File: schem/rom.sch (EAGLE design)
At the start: 14 parts, among them IC10 74HC32N, IC11 74HC32N, IC12 74HC32N, IC13 74HC32N, IC14 74HC04N, IC6 74HC374N, IC7 74HC08N, IC8 74HC377N, IC9 74HC377N

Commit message: progress
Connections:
- net IRQ renamed /IRQ
- new net SYNC: IC7D.O
- net /BUSACK: now also IC7D.I0
- net FETCH: now also IC7D.I1
- net INVF: no longer IC7C.O
- net INVF0: now also IC7C.O
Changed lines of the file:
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@@
 <instance part="IC13" gate="B" x="269.24" y="-15.24"/>
 <instance part="IC13" gate="C" x="154.94" y="-20.32"/>
+<instance part="IC7" gate="D" x="228.6" y="20.32"/>
 </instances>
 <busses>
@@
 </segment>
 </net>
-<net name="IRQ" class="0">
+<net name="/IRQ" class="0">
 <segment>
 <pinref part="IC6" gate="A" pin="4D"/>
@@
 <wire x1="220.98" y1="48.26" x2="210.82" y2="48.26" width="0.1524" layer="91"/>
 <label x="210.82" y="48.26" size="1.778" layer="95"/>
+</segment>
+<segment>
+<pinref part="IC7" gate="D" pin="I0"/>
+<wire x1="220.98" y1="22.86" x2="210.82" y2="22.86" width="0.1524" layer="91"/>
+<label x="210.82" y="22.86" size="1.778" layer="95"/>
 </segment>
 </net>
@@
 <label x="276.86" y="45.72" size="1.778" layer="95"/>
 </segment>
+<segment>
+<pinref part="IC7" gate="D" pin="I1"/>
+<wire x1="220.98" y1="17.78" x2="213.36" y2="17.78" width="0.1524" layer="91"/>
+<label x="213.36" y="17.78" size="1.778" layer="95"/>
+</segment>
 </net>
 <net name="/INRES" class="0">
@@
 <label x="226.06" y="83.82" size="1.778" layer="95"/>
 </segment>
+<segment>
+<pinref part="IC7" gate="C" pin="O"/>
+<wire x1="236.22" y1="33.02" x2="246.38" y2="33.02" width="0.1524" layer="91"/>
+<label x="236.22" y="33.02" size="1.778" layer="95"/>
+</segment>
 </net>
 <net name="INVF" class="0">
@@
 <label x="264.16" y="83.82" size="1.778" layer="95"/>
 </segment>
-<segment>
-<pinref part="IC7" gate="C" pin="O"/>
-<wire x1="236.22" y1="33.02" x2="246.38" y2="33.02" width="0.1524" layer="91"/>
-<label x="236.22" y="33.02" size="1.778" layer="95"/>
-</segment>
-</net>
+</net>
+<net name="SYNC" class="0">
+<segment>
+<pinref part="IC7" gate="D" pin="O"/>
+<wire x1="236.22" y1="20.32" x2="243.84" y2="20.32" width="0.1524" layer="91"/>
+<label x="236.22" y="20.32" size="1.778" layer="95"/>
+</segment>
+</net>

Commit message: board changes ; rom schematic finished
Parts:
- added SV1, SV3, SV4, SV6, SV7, SV8: (no value), con-lstb:MA08-1
- added SV10, SV2, SV5, SV9: (no value), con-lstb:MA06-1
- added SV11, SV12, SV13: (no value), con-lstb:MA05-2
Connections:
- removed net IBS0: IC2A.O0
- removed net IBS1: IC2A.O1
- removed net IBS2: IC2A.O2
- removed net IBS3: IC2A.O3
- new net IB0: SV1.1
- new net IB1: SV1.2
- new net IB2: SV1.3
- new net IB3: SV1.4
- new net IB4: SV1.5
- new net IB5: SV1.6
- new net IB6: SV1.7
- new net IB7: SV1.8
- new net IBR0: IC2A.O0, SV10.3
- new net IBR1: IC2A.O1, SV10.4
- new net IBR2: IC2A.O2, SV10.5
- new net IBR3: IC2A.O3, SV10.6
- new net OB0: SV4.1
- new net OB1: SV4.2
- new net OB2: SV4.3
- new net OB3: SV4.4
- new net OB4: SV4.5
- new net OB5: SV4.6
- new net OB6: SV4.7
- new net OB7: SV4.8
- net /BUSACK: now also SV9.2
- net /BUSREQ: now also SV9.3
- net /INRES: now also SV12.3
- net /IRQ: now also SV9.6
- net /WE: now also SV9.4
- net ABHS0: now also SV11.2
- net ABHS1: now also SV11.4
- net ABHS2: now also SV11.6
- net ABLS0: now also SV12.2
- net ABLS1: now also SV12.4
- net ABLS2: now also SV12.6
- net ALUC: now also SV8.3
- net BUSACK: now also SV9.1
- net CIN: now also SV6.8
- net CLK: now also SV2.3
- net COND: now also SV8.7
- net DB0: now also SV3.1
- net DB1: now also SV3.2
- net DB2: now also SV3.3
- net DB3: now also SV3.4
- net DB4: now also SV3.5
- net DB5: now also SV3.6
- net DB6: now also SV3.7
- net DB7: now also SV3.8
- net DP: now also SV12.1
- net F0: now also SV6.1
- net F1: now also SV6.2
- net F2: now also SV6.3
- net F3: now also SV6.4
- net F4: now also SV6.5
- net F5: now also SV6.6
- net FL0: now also SV7.1
- net FL1: now also SV7.2
- net FL2: now also SV7.3
- net FL3: now also SV7.4
- net FL4: now also SV7.5
- net FL5: now also SV7.6
- net FL6: now also SV7.7
- net FL7: now also SV7.8
- net FL8: now also SV8.1
- net FL9: now also SV8.2
- net GND: now also IC13D.I0, IC13D.I1, IC14F.I, SV11.10, SV11.9, SV12.10, SV12.5, SV12.7, SV12.9, SV13.10, SV13.9, SV2.4, SV2.5, SV2.6, SV5.4, SV5.5, SV5.6, SV8.8
- net IN0: now also SV13.1
- net IN1: now also SV13.2
- net IN2: now also SV13.3
- net IN3: now also SV13.4
- net IN4: now also SV13.5
- net IN5: now also SV13.6
- net IN6: now also SV13.7
- net IN7: now also SV13.8
- net INIRQ: now also SV8.6
- net INVF: now also SV6.7
- net OBS0: now also SV11.1
- net OBS1: now also SV11.3
- net OBS2: now also SV11.5
- net OBS3: now also SV11.7
- net PCP: now also SV11.8, SV12.8
- net PQ0: now also SV8.4
- net PQ2: now also SV8.5
- net RESET: now also SV10.1
- net SYNC: now also SV10.2
- net VCC: now also SV2.1, SV2.2, SV5.1, SV5.2, SV5.3
- net WR: now also SV9.5

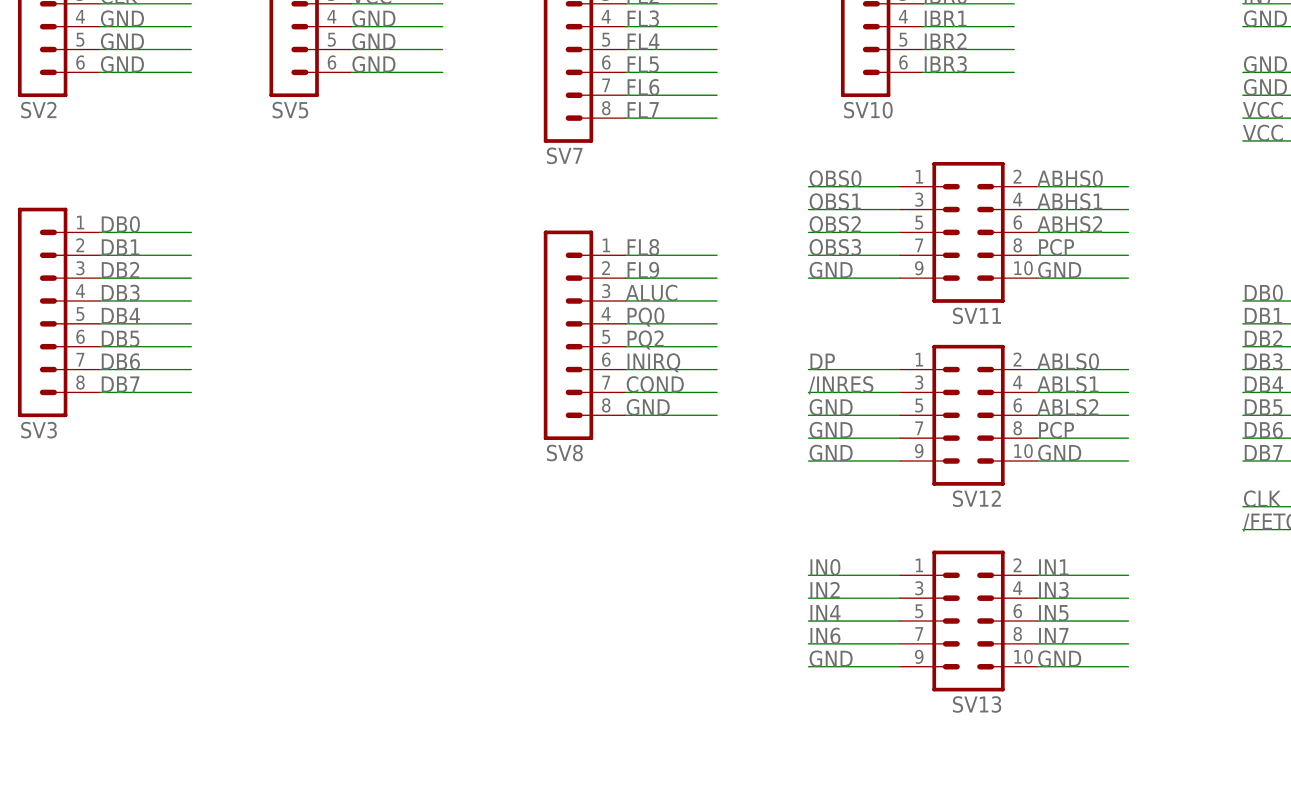
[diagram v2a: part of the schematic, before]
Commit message: adapted schematics for single headers
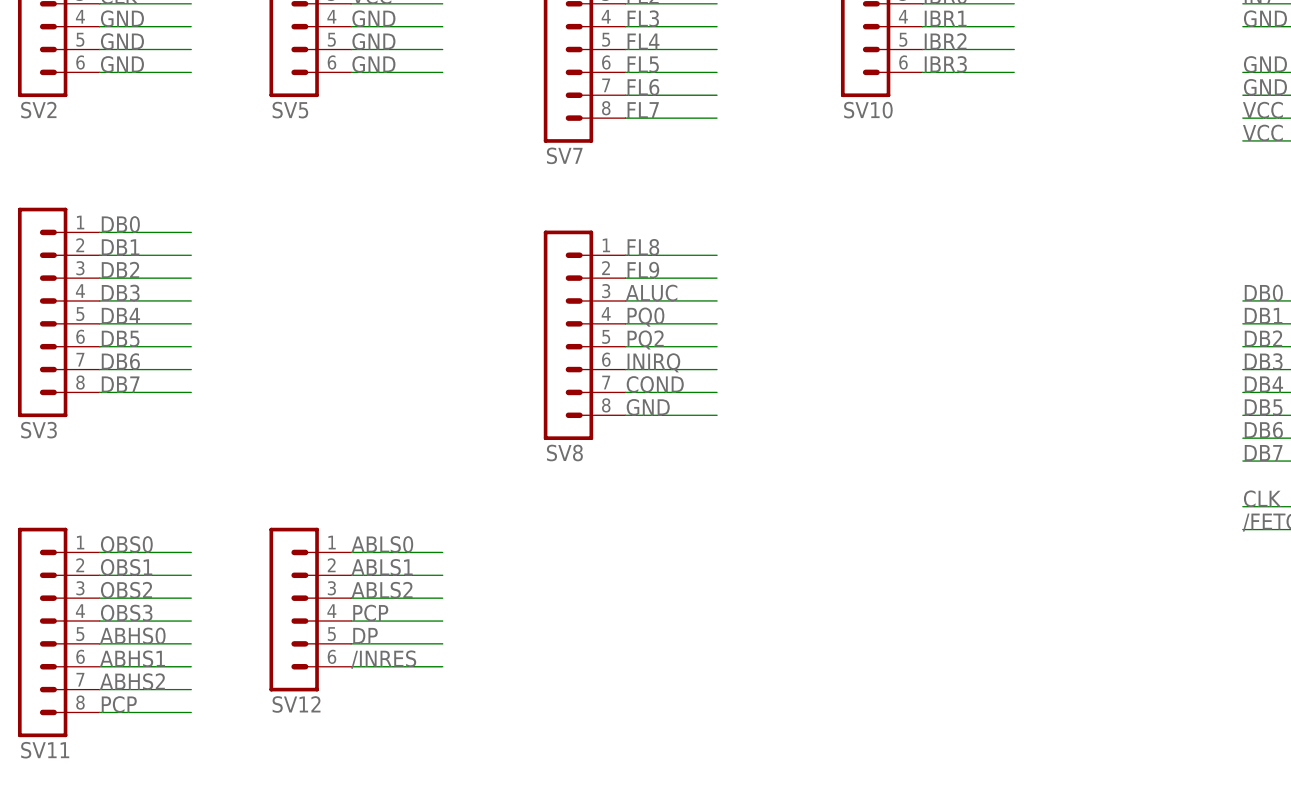
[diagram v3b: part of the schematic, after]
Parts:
- removed SV13: (no value), con-lstb:MA05-2
- SV11: device con-lstb:MA05-2 -> con-lstb:MA08-1
- SV12: device con-lstb:MA05-2 -> con-lstb:MA06-1
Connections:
- net /INRES: now also SV12.6; no longer SV12.3
- net ABHS0: now also SV11.5; no longer SV11.2
- net ABHS1: now also SV11.6; no longer SV11.4
- net ABHS2: now also SV11.7; no longer SV11.6
- net ABLS0: now also SV12.1; no longer SV12.2
- net ABLS1: now also SV12.2; no longer SV12.4
- net ABLS2: now also SV12.3; no longer SV12.6
- net DP: now also SV12.5; no longer SV12.1
- net GND: no longer SV11.10, SV11.9, SV12.10, SV12.5, SV12.7, SV12.9, SV13.10, SV13.9
- net IN0: no longer SV13.1
- net IN1: no longer SV13.2
- net IN2: no longer SV13.3
- net IN3: no longer SV13.4
- net IN4: no longer SV13.5
- net IN5: no longer SV13.6
- net IN6: no longer SV13.7
- net IN7: no longer SV13.8
- net OBS1: now also SV11.2; no longer SV11.3
- net OBS2: now also SV11.3; no longer SV11.5
- net OBS3: now also SV11.4; no longer SV11.7
- net PCP: now also SV12.4; no longer SV12.8

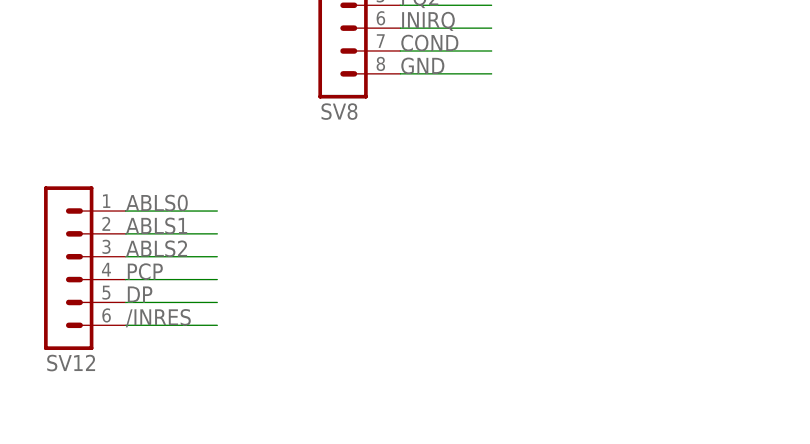
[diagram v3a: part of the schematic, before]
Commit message: added debugging pins to rom board
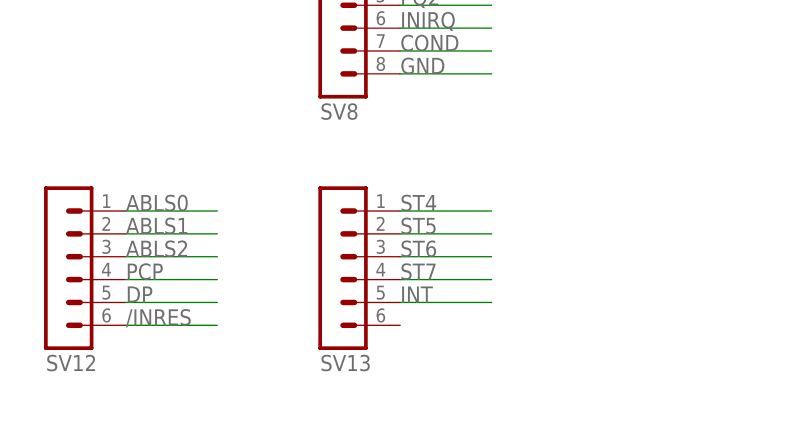
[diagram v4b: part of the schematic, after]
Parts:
- added SV13: (no value), con-lstb:MA06-1
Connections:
- net INT: now also SV13.5
- net ST4: now also SV13.1
- net ST5: now also SV13.2
- net ST6: now also SV13.3
- net ST7: now also SV13.4
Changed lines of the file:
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@@
 <part name="SV11" library="con-lstb" deviceset="MA08-1" device=""/>
 <part name="SV12" library="con-lstb" deviceset="MA06-1" device=""/>
+<part name="SV13" library="con-lstb" deviceset="MA06-1" device=""/>
 </parts>
 <sheets>
@@
 <instance part="SV11" gate="1" x="-129.54" y="-12.7" rot="MR180"/>
 <instance part="SV12" gate="1" x="-101.6" y="-12.7" rot="MR180"/>
+<instance part="SV13" gate="1" x="-71.12" y="-12.7" rot="MR180"/>
 </instances>
 <busses>
@@
 <label x="132.08" y="22.86" size="1.778" layer="95"/>
 </segment>
+<segment>
+<pinref part="SV13" gate="1" pin="1"/>
+<wire x1="-63.5" y1="-5.08" x2="-53.34" y2="-5.08" width="0.1524" layer="91"/>
+<label x="-63.5" y="-5.08" size="1.778" layer="95"/>
+</segment>
 </net>
 <net name="ST5" class="0">
@@
 <label x="132.08" y="17.78" size="1.778" layer="95"/>
 </segment>
+<segment>
+<pinref part="SV13" gate="1" pin="2"/>
+<wire x1="-63.5" y1="-7.62" x2="-53.34" y2="-7.62" width="0.1524" layer="91"/>
+<label x="-63.5" y="-7.62" size="1.778" layer="95"/>
+</segment>
 </net>
 <net name="ST6" class="0">
@@
 <label x="132.08" y="7.62" size="1.778" layer="95"/>
 </segment>
+<segment>
+<pinref part="SV13" gate="1" pin="3"/>
+<wire x1="-63.5" y1="-10.16" x2="-53.34" y2="-10.16" width="0.1524" layer="91"/>
+<label x="-63.5" y="-10.16" size="1.778" layer="95"/>
+</segment>
 </net>
 <net name="ST7" class="0">
@@
 <wire x1="132.08" y1="2.54" x2="139.7" y2="2.54" width="0.1524" layer="91"/>
 <label x="132.08" y="2.54" size="1.778" layer="95"/>
+</segment>
+<segment>
+<pinref part="SV13" gate="1" pin="4"/>
+<wire x1="-63.5" y1="-12.7" x2="-53.34" y2="-12.7" width="0.1524" layer="91"/>
+<label x="-63.5" y="-12.7" size="1.778" layer="95"/>
 </segment>
 </net>
@@
 <label x="276.86" y="7.62" size="1.778" layer="95"/>
 </segment>
-</net>
+<segment>
+<pinref part="SV13" gate="1" pin="5"/>
+<wire x1="-63.5" y1="-15.24" x2="-53.34" y2="-15.24" width="0.1524" layer="91"/>
+<label x="-63.5" y="-15.24" size="1.778" layer="95"/>
+</segment>
+</net>

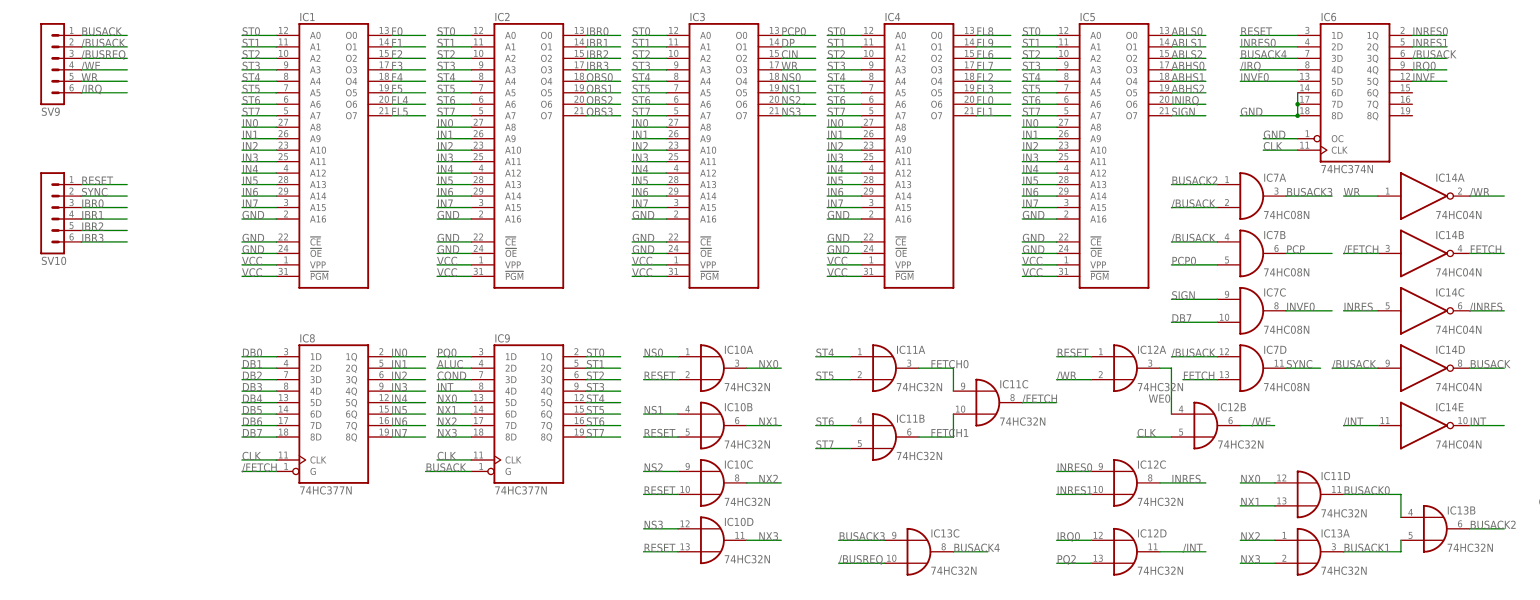
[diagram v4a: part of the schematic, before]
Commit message: added synchronizer to reset line
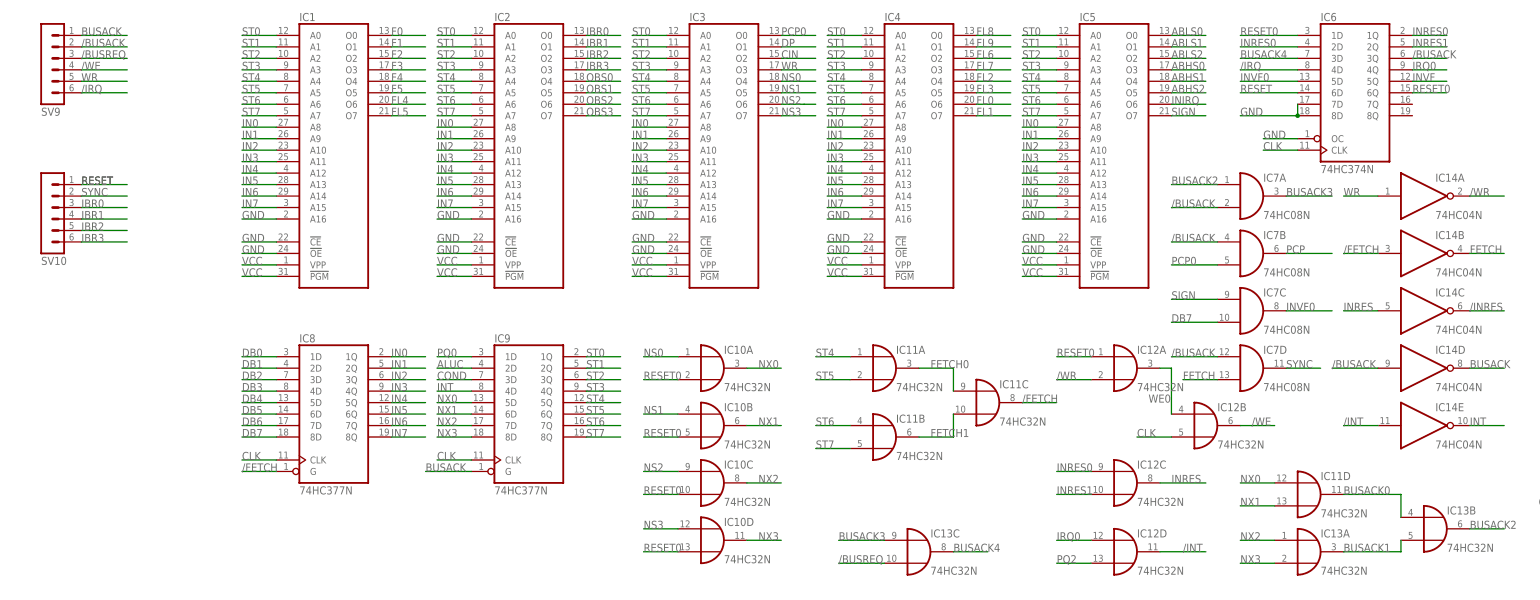
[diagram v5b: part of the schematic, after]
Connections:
- new net RESET0: IC10A.I1, IC10B.I1, IC10C.I1, IC10D.I1, IC12A.I0, IC6A.1D, IC6A.6Q
- net GND: no longer IC6A.6D
- net RESET: now also IC6A.6D; no longer IC10A.I1, IC10B.I1, IC10C.I1, IC10D.I1, IC12A.I0, IC6A.1D
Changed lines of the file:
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@@
 <wire x1="238.76" y1="76.2" x2="226.06" y2="76.2" width="0.1524" layer="91"/>
 <label x="226.06" y="76.2" size="1.778" layer="95"/>
-<pinref part="IC6" gate="A" pin="6D"/>
 <pinref part="IC6" gate="A" pin="7D"/>
-<wire x1="238.76" y1="78.74" x2="238.76" y2="81.28" width="0.1524" layer="91"/>
 <wire x1="238.76" y1="78.74" x2="238.76" y2="76.2" width="0.1524" layer="91"/>
 <junction x="238.76" y="76.2"/>
-<junction x="238.76" y="78.74"/>
 </segment>
 <segment>
@@
 </segment>
 </net>
-<net name="RESET" class="0">
+<net name="RESET0" class="0">
 <segment>
 <pinref part="IC6" gate="A" pin="1D"/>
@@
 </segment>
 <segment>
-<pinref part="SV10" gate="1" pin="1"/>
-<wire x1="-30.48" y1="60.96" x2="-20.32" y2="60.96" width="0.1524" layer="91"/>
-<label x="-30.48" y="60.96" size="1.778" layer="95"/>
+<pinref part="IC6" gate="A" pin="6Q"/>
+<wire x1="264.16" y1="81.28" x2="271.78" y2="81.28" width="0.1524" layer="91"/>
+<label x="264.16" y="81.28" size="1.778" layer="95"/>
 </segment>
 </net>
@@
 </segment>
 </net>
+<net name="RESET" class="0">
+<segment>
+<pinref part="IC6" gate="A" pin="6D"/>
+<wire x1="238.76" y1="81.28" x2="226.06" y2="81.28" width="0.1524" layer="91"/>
+<label x="226.06" y="81.28" size="1.778" layer="95"/>
+</segment>
+<segment>
+<pinref part="SV10" gate="1" pin="1"/>
+<wire x1="-30.48" y1="60.96" x2="-20.32" y2="60.96" width="0.1524" layer="91"/>
+<label x="-30.48" y="60.96" size="1.778" layer="95"/>
+<label x="-30.48" y="60.96" size="1.778" layer="95"/>
+</segment>
+</net>
